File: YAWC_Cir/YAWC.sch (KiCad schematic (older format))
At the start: 10 parts, among them P1 JST-PH_2, U1 TPS769XX, U3 MMA845Q

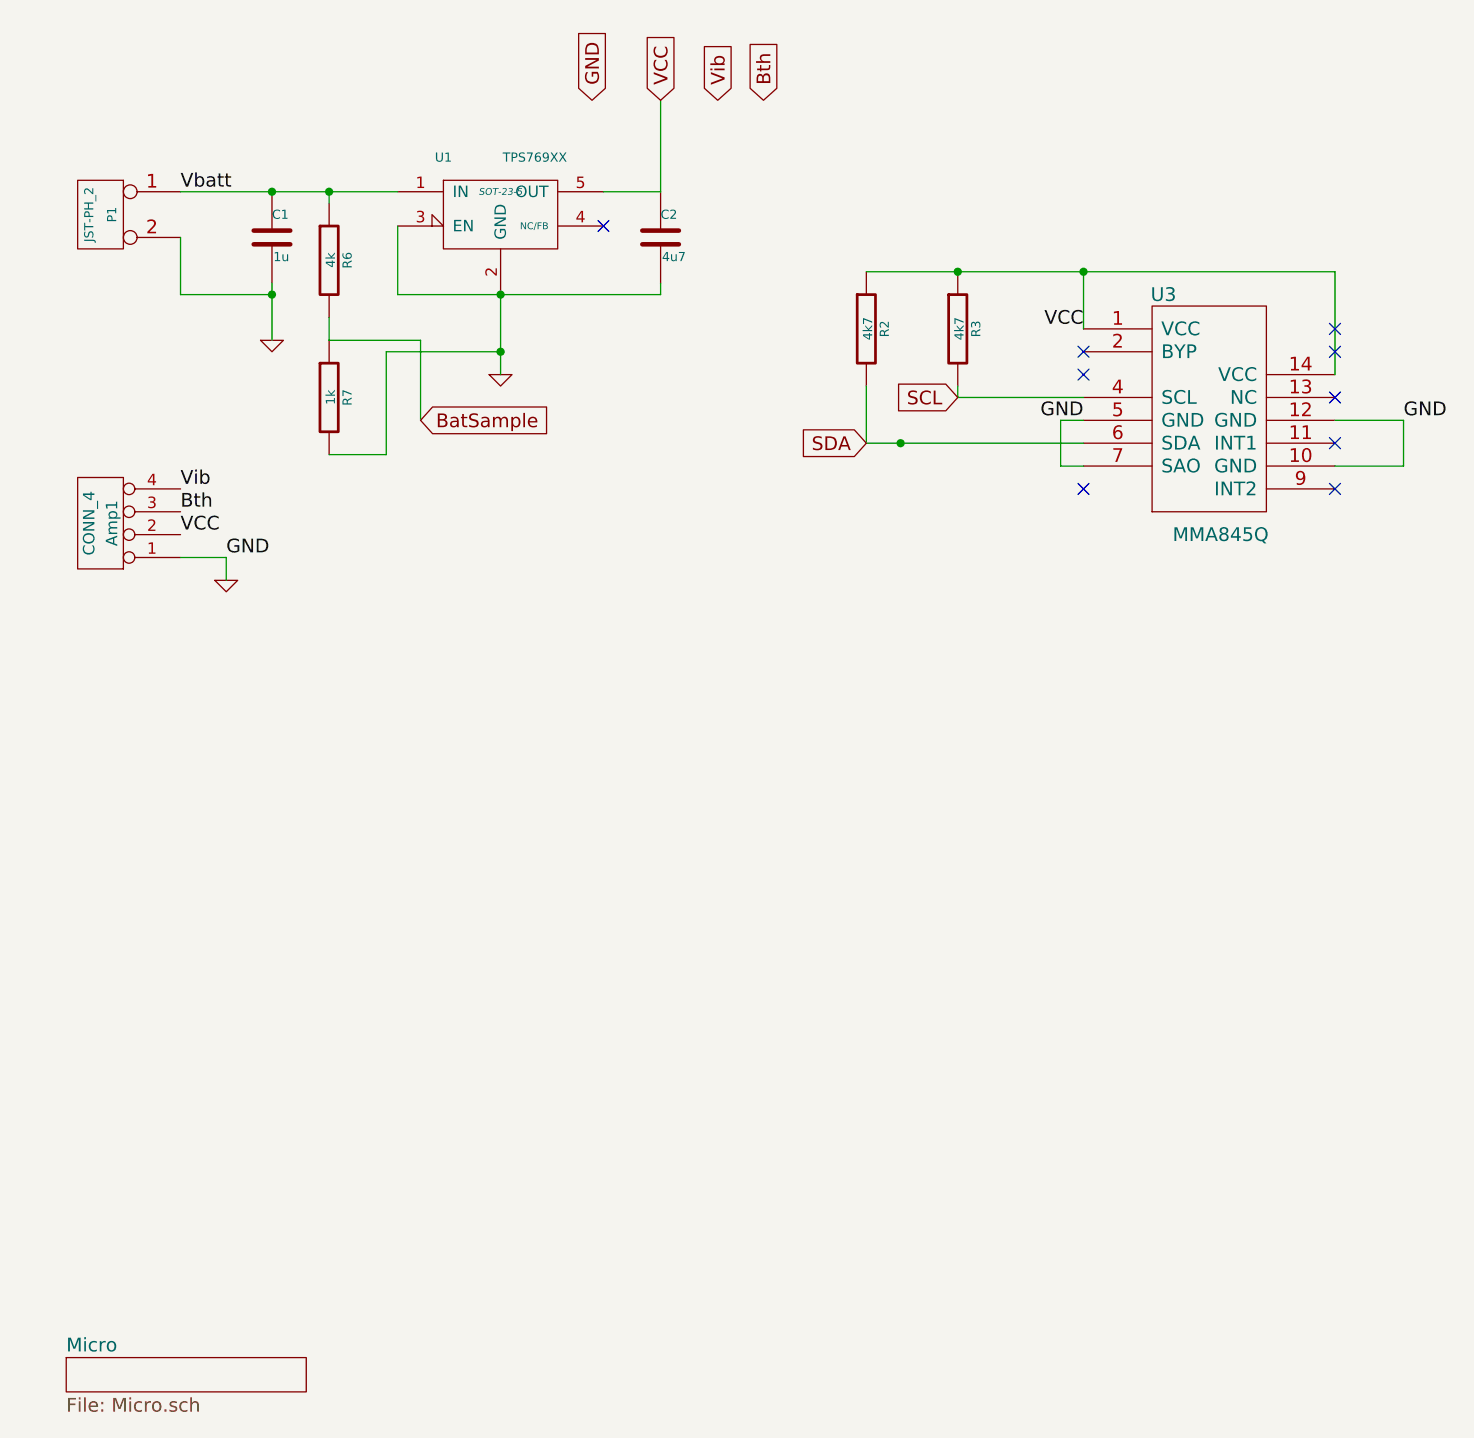
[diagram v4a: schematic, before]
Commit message: Schematic for version with finger boards done. Parts matched.
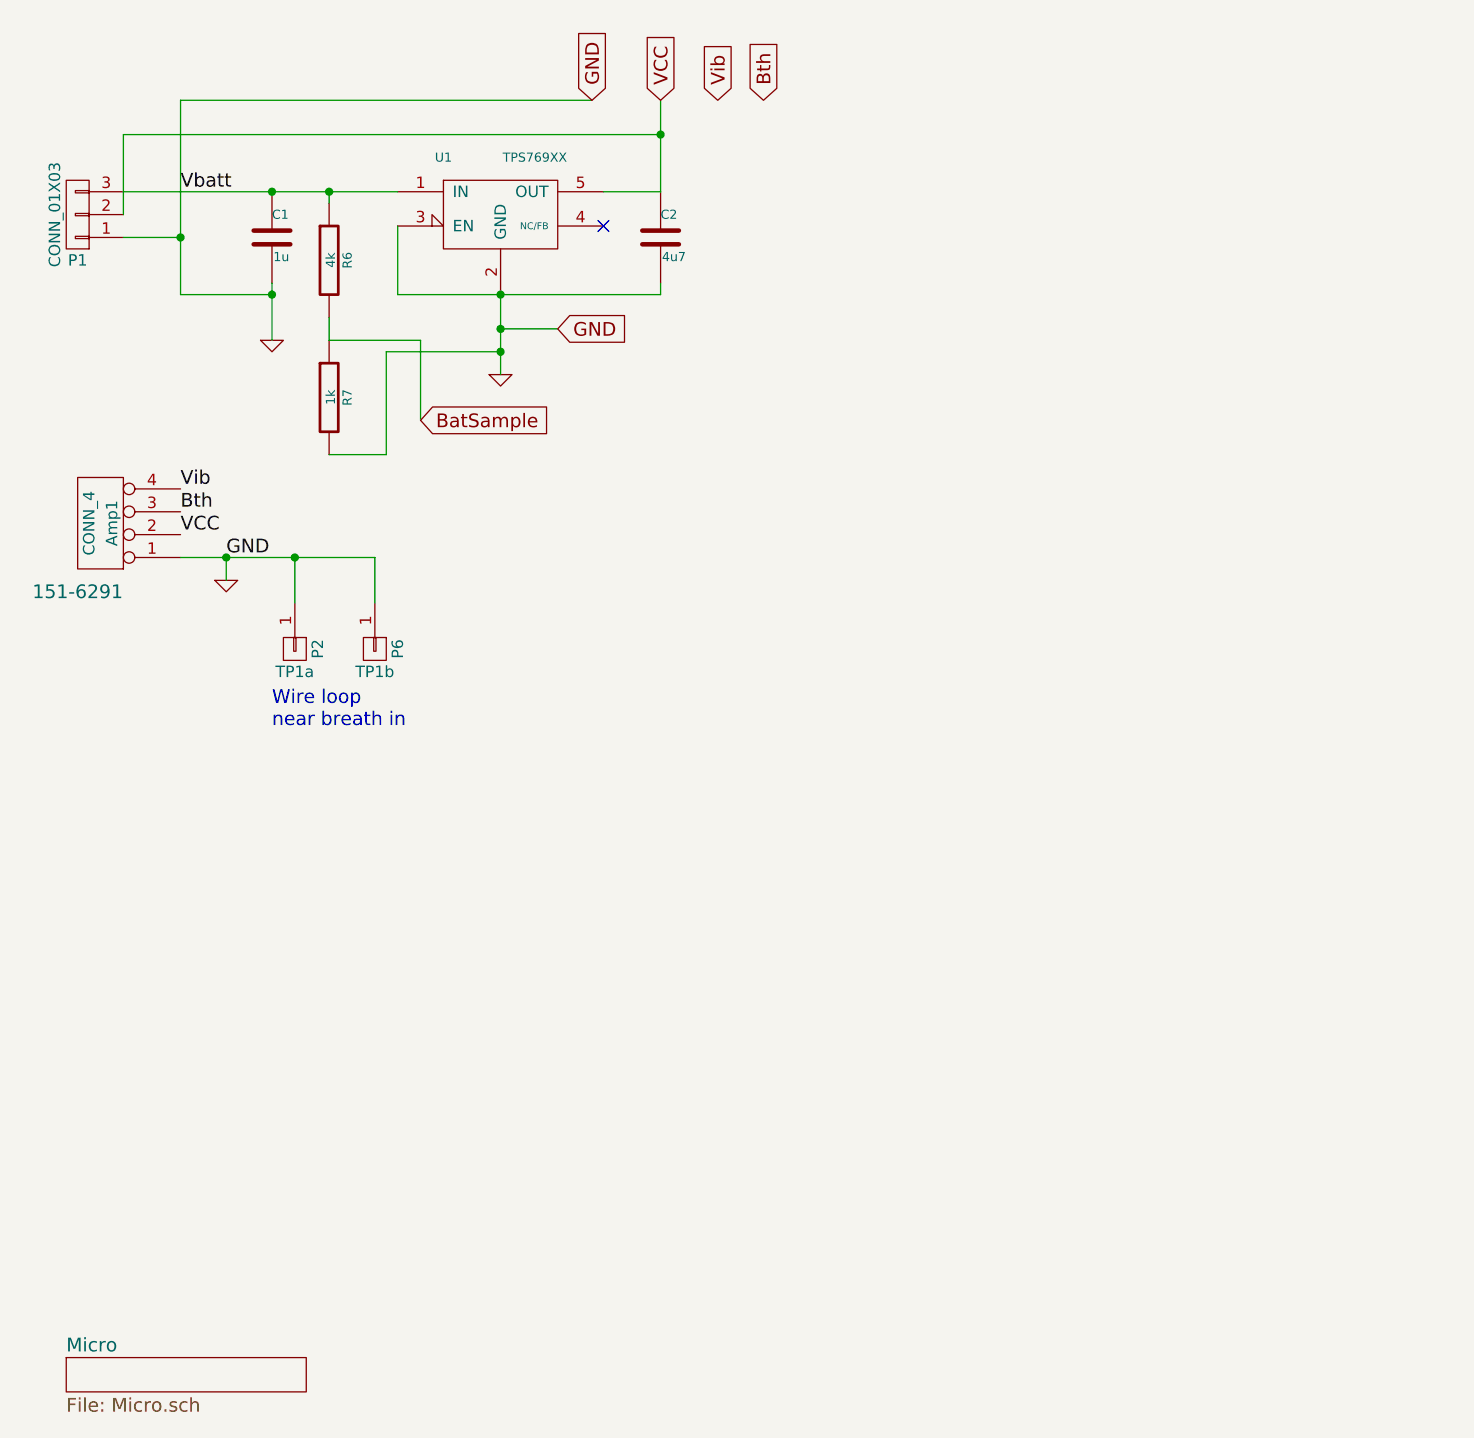
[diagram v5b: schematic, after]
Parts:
- removed P1: JST-PH_2, symbol CONN_2
- removed R2, R3: 4k7, symbol R-RESCUE-YAWC
- removed U3: MMA845Q, symbol MMA845Q
- added P1: CONN_01X03, JST:S3B-XH, symbol CONN_01X03
- added P2: TP1a, PIN_Hdr:Pin_Header_Straight_1x01, symbol CONN_01X01
- added P6: TP1b, PIN_Hdr:Pin_Header_Straight_1x01, symbol CONN_01X01
- Amp1: footprint (none) -> JST:S4B-XH; ManPart (none) -> S4B-XH-A; PartNo (none) -> 151-6291
- C1, C2: footprint (none) -> Capacitors_SMD:C_1206_HandSoldering
- R6, R7: footprint (none) -> Resistors_SMD:R_0805_HandSoldering
- U1: footprint SOT-23-5 -> TO_SOT_Packages_SMD:SOT-23-5
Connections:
- net Vbatt is gone; now on net GND: C1.1, R6.1, U1.1 (IN)
- net GND: now also P1.1 (P1), P1.3 (P3), P2.1 (P1), P6.1 (P1)
- net VCC: now also P1.2 (P2)
- no-connect marks 9 -> 1
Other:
- note added: "Wire loop \nnear breath in"
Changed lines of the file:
@@
 $EndDescr
-$Comp
-L CONN_2 P1
-U 1 1 538F66AD
-P 1450 1650
-F 0 "P1" V 1400 1650 40  0000 C CNN
-F 1 "JST-PH_2" V 1500 1650 40  0000 C CNN
-F 2 "" H 1450 1650 60  0000 C CNN
-F 3 "" H 1450 1650 60  0000 C CNN
-	1    1450 1650
-	-1   0    0    -1
-$EndComp
 $Comp
 L TPS769XX-RESCUE-YAWC U1
@@
 F 0 "U1" H 2950 2000 40  0000 C CNN
 F 1 "TPS769XX" H 3350 2000 40  0000 C CNN
-F 2 "SOT-23-5" H 3200 1850 30  0000 C CIN
+F 2 "TO_SOT_Packages_SMD:SOT-23-5" H 3200 1850 30  0001 C CIN
 F 3 "" H 3200 1700 60  0000 C CNN
 	1    3200 1700
@@
 F 0 "C1" H 2200 1850 40  0000 L CNN
 F 1 "1u" H 2206 1665 40  0000 L CNN
-F 2 "" H 2238 1600 30  0000 C CNN
+F 2 "Capacitors_SMD:C_1206_HandSoldering" H 2238 1600 30  0001 C CNN
 F 3 "" H 2200 1750 60  0000 C CNN
 	1    2200 1750
@@
 	2200 1950 2200 2200
 Wire Wire Line
-	1800 2000 1800 1750
+	1800 1150 1800 2000
 Connection ~ 2200 2000
 Text Label 1800 1550 0    60   ~ 0
@@
 F 0 "C2" H 3900 1850 40  0000 L CNN
 F 1 "4u7" H 3906 1665 40  0000 L CNN
-F 2 "" H 3938 1600 30  0000 C CNN
+F 2 "Capacitors_SMD:C_1206_HandSoldering" H 3938 1600 30  0001 C CNN
 F 3 "" H 3900 1750 60  0000 C CNN
 	1    3900 1750
@@
 F 0 "Amp1" V 1400 3000 50  0000 C CNN
 F 1 "CONN_4" V 1500 3000 50  0000 C CNN
-F 2 "" H 1450 3000 60  0000 C CNN
+F 2 "JST:S4B-XH" H 1450 3000 60  0001 C CNN
 F 3 "" H 1450 3000 60  0000 C CNN
+F 4 "151-6291" H 1550 3300 60  0000 C CNN "PartNo"
+F 5 "S4B-XH-A" V 1450 3000 60  0001 C CNN "ManPart"
 	1    1450 3000
 	-1   0    0    1
@@
 Text GLabel 4350 1150 1    60   Input ~ 0
 Bth
-$Comp
-L MMA845Q U3
-U 1 1 539AF65E
-P 6250 2650
-F 0 "U3" H 6100 3300 60  0000 C CNN
-F 1 "MMA845Q" H 6350 2250 60  0000 C CNN
-F 2 "" H 6250 2650 60  0000 C CNN
-F 3 "" H 6250 2650 60  0000 C CNN
-	1    6250 2650
-	1    0    0    -1
-$EndComp
-Text Label 5750 2150 2    60   ~ 0
-VCC
-Text Label 5750 2550 2    60   ~ 0
-GND
-Text Label 7150 2550 0    60   ~ 0
-GND
-Wire Wire Line
-	6850 2550 7150 2550
-Wire Wire Line
-	6850 2750 7150 2750
-Wire Wire Line
-	7150 2750 7150 2550
-$Comp
-L R-RESCUE-YAWC R3
-U 1 1 539AF7E0
-P 5200 2150
-F 0 "R3" V 5280 2150 40  0000 C CNN
-F 1 "4k7" V 5207 2151 40  0000 C CNN
-F 2 "" V 5130 2150 30  0000 C CNN
-F 3 "" H 5200 2150 30  0000 C CNN
-	1    5200 2150
-	1    0    0    -1
-$EndComp
-$Comp
-L R-RESCUE-YAWC R2
-U 1 1 539AF849
-P 4800 2150
-F 0 "R2" V 4880 2150 40  0000 C CNN
-F 1 "4k7" V 4807 2151 40  0000 C CNN
-F 2 "" V 4730 2150 30  0000 C CNN
-F 3 "" H 4800 2150 30  0000 C CNN
-	1    4800 2150
-	1    0    0    -1
-$EndComp
-Wire Wire Line
-	4800 1900 6850 1900
-Wire Wire Line
-	5750 1900 5750 2150
-Connection ~ 5200 1900
-Wire Wire Line
-	5200 2400 5200 2450
-Wire Wire Line
-	5200 2450 5750 2450
-Wire Wire Line
-	4800 2650 5750 2650
-Wire Wire Line
-	5750 2750 5650 2750
-Wire Wire Line
-	5650 2750 5650 2550
-Wire Wire Line
-	5650 2550 5750 2550
-Wire Wire Line
-	6850 1900 6850 2350
-Connection ~ 5750 1900
-Text GLabel 4800 2650 0    60   Input ~ 0
-SDA
-Text GLabel 5200 2450 0    60   Input ~ 0
-SCL
-Wire Wire Line
-	4800 2400 4800 2650
-Connection ~ 4950 2650
-NoConn ~ 6850 2450
-NoConn ~ 6850 2650
-NoConn ~ 6850 2850
 NoConn ~ 3650 1700
-NoConn ~ 5750 2350
-NoConn ~ 6850 2250
-NoConn ~ 6850 2150
-NoConn ~ 5750 2850
-NoConn ~ 5750 2250
-Wire Wire Line
-	1800 3150 2000 3150
+Wire Wire Line
+	1800 3150 2650 3150
 Wire Wire Line
 	3200 2000 3200 2350
@@
 Connection ~ 3200 2000
 Wire Wire Line
-	1800 1550 2750 1550
+	1550 1550 2750 1550
 $Comp
 L R-RESCUE-YAWC R6
@@
 F 0 "R6" V 2530 1850 40  0000 C CNN
 F 1 "4k" V 2457 1851 40  0000 C CNN
-F 2 "" V 2380 1850 30  0000 C CNN
+F 2 "Resistors_SMD:R_0805_HandSoldering" V 2380 1850 30  0001 C CNN
 F 3 "" H 2450 1850 30  0000 C CNN
 	1    2450 1850
@@
 F 0 "R7" V 2530 2450 40  0000 C CNN
 F 1 "1k" V 2457 2451 40  0000 C CNN
-F 2 "" V 2380 2450 30  0000 C CNN
+F 2 "Resistors_SMD:R_0805_HandSoldering" V 2380 2450 30  0001 C CNN
 F 3 "" H 2450 2450 30  0000 C CNN
 	1    2450 2450
@@
 Wire Wire Line
 	2850 2200 2850 2550
+$Comp
+L CONN_01X03 P1
+U 1 1 56C62FA6
+P 1350 1650
+F 0 "P1" H 1350 1850 50  0000 C CNN
+F 1 "CONN_01X03" V 1450 1650 50  0000 C CNN
+F 2 "JST:S3B-XH" H 1350 1650 50  0001 C CNN
+F 3 "" H 1350 1650 50  0000 C CNN
+	1    1350 1650
+	-1   0    0    1
+$EndComp
+Wire Wire Line
+	1800 1750 1550 1750
+Wire Wire Line
+	1550 1650 1550 1300
+Wire Wire Line
+	1550 1300 3900 1300
+Connection ~ 3900 1300
+$Comp
+L CONN_01X01 P6
+U 1 1 56C86765
+P 2650 3550
+F 0 "P6" H 2650 3650 50  0000 C CNN
+F 1 "TP1b" V 2750 3550 50  0000 C CNN
+F 2 "PIN_Hdr:Pin_Header_Straight_1x01" H 2650 3550 50  0001 C CNN
+F 3 "" H 2650 3550 50  0000 C CNN
+	1    2650 3550
+	0    1    1    0
+$EndComp
+$Comp
+L CONN_01X01 P2
+U 1 1 56C867E8
+P 2300 3550
+F 0 "P2" H 2300 3650 50  0000 C CNN
+F 1 "TP1a" V 2400 3550 50  0000 C CNN
+F 2 "PIN_Hdr:Pin_Header_Straight_1x01" H 2300 3550 50  0001 C CNN
+F 3 "" H 2300 3550 50  0000 C CNN
+	1    2300 3550
+	0    1    1    0
+$EndComp
+Wire Wire Line
+	2650 3150 2650 3350
+Wire Wire Line
+	2300 3150 2300 3350
+Connection ~ 2300 3150
+Connection ~ 2000 3150
+Text Notes 2200 3900 0    60   ~ 0
+Wire loop \nnear breath in
+Text GLabel 3450 2150 2    60   Input ~ 0
+GND
+Wire Wire Line
+	3200 2150 3450 2150
+Connection ~ 3200 2150
+Wire Wire Line
+	3600 1150 1800 1150
+Connection ~ 1800 1750
 $EndSCHEMATC

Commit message: More work on main PCB and positioned connectors to match Keys
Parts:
- Amp1: footprint JST:S4B-XH -> PIN_Hdr:Pin_Header_Straight_1x04
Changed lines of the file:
@@
 F 0 "Amp1" V 1400 3000 50  0000 C CNN
 F 1 "CONN_4" V 1500 3000 50  0000 C CNN
-F 2 "JST:S4B-XH" H 1450 3000 60  0001 C CNN
+F 2 "PIN_Hdr:Pin_Header_Straight_1x04" H 1450 3000 60  0001 C CNN
 F 3 "" H 1450 3000 60  0000 C CNN
 F 4 "151-6291" H 1550 3300 60  0000 C CNN "PartNo"

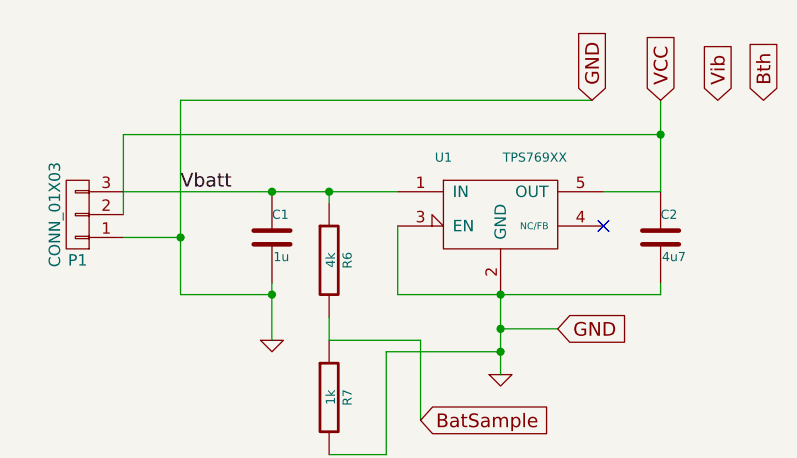
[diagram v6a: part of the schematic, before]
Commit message: move parts nearer final positions
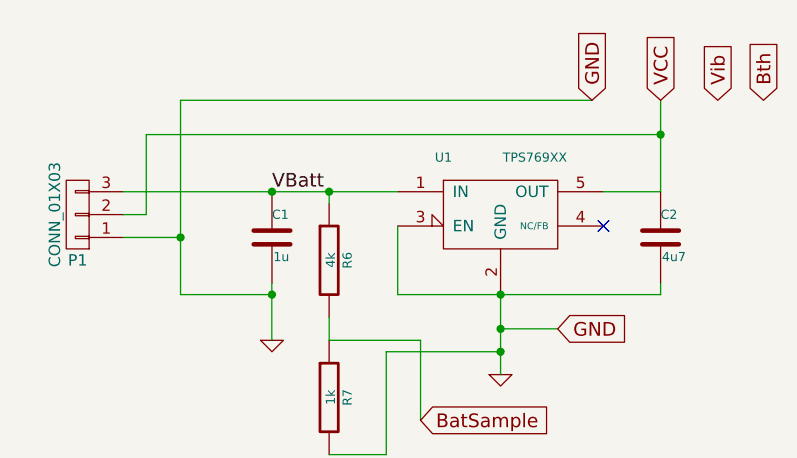
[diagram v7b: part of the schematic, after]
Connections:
- net GND: no longer C1.1, P1.3 (P3), R6.1, U1.1 (IN)
- new net VBatt: C1.1, P1.3 (P3), R6.1, U1.1 (IN)
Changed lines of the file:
@@
 	1800 1150 1800 2000
 Connection ~ 2200 2000
-Text Label 1800 1550 0    60   ~ 0
-Vbatt
 Text GLabel 3900 1150 1    60   Input ~ 0
 VCC
@@
 Wire Wire Line
 	1800 1750 1550 1750
-Wire Wire Line
-	1550 1650 1550 1300
-Wire Wire Line
-	1550 1300 3900 1300
 Connection ~ 3900 1300
 $Comp
@@
 	3600 1150 1800 1150
 Connection ~ 1800 1750
+Wire Wire Line
+	1550 1650 1650 1650
+Wire Wire Line
+	1650 1650 1650 1300
+Wire Wire Line
+	1650 1300 3900 1300
+Text Label 2200 1550 0    60   ~ 0
+VBatt
 $EndSCHEMATC
